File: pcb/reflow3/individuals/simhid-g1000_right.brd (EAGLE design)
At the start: 35 x 192 mm, 75 parts, among them J4 PCB-INTERCONNECT, J5 USB4145-03-0230-CHS, J6 2212S, SW27 SLLB510100-HS, SW28 TS-1109S-B-B, SW29 TS-1109S-B-B, SW30 TS-1109S-B-B, SW31 TS-1109S-B-B, SW32 TS-1109S-B-B, SW33 TS-1109S-B-B, SW34 TS-1109S-B-B, U4 STM32F411CCU, U5 MCP23S18-E/MJ, U6 MCP1703AT-3302E/CB, X1 16MHz/10pF

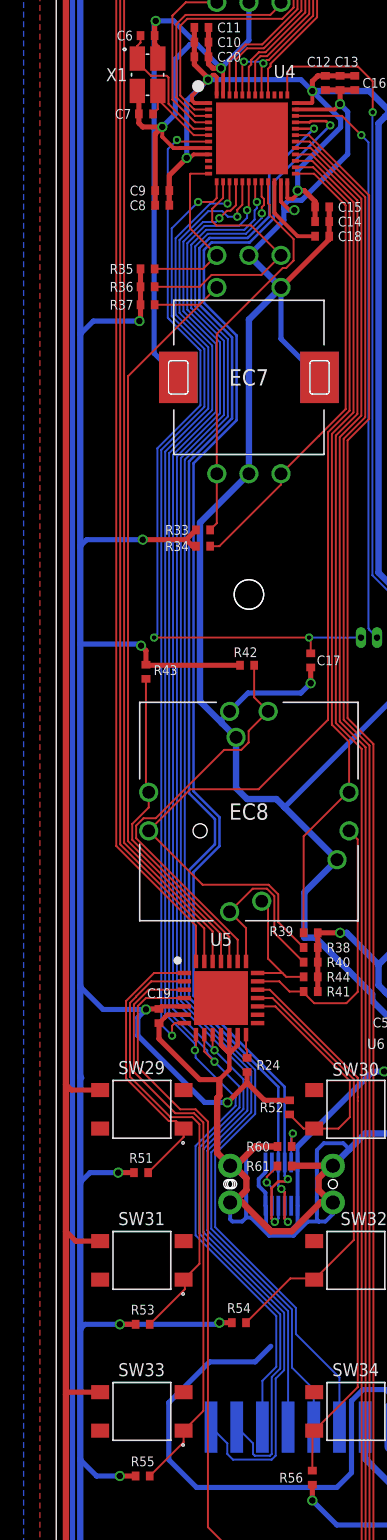
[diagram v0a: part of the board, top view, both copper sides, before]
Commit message: improved the artwork for the new variant
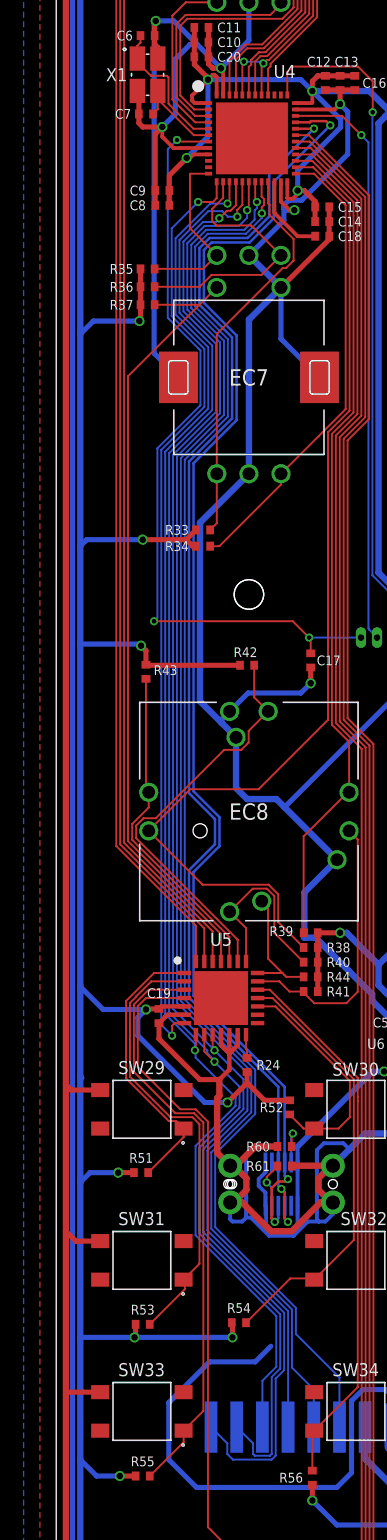
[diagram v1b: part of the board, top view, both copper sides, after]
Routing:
- net +3V3: track 611.1 -> 611.9 mm
- net NRST: track 61.5 -> 60.7 mm
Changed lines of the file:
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@@
 </layers>
 <board>
-<fusionsync huburn="a.cGVyc29uYWw6dWUyYmE2M2My" projecturn="a.cGVyc29uYWw6dWUyYmE2M2MyIzIwMTgwOTE3MTQ5MTY5Mjgx" f3durn="urn:adsk.wipprod:dm.lineage:6ddGwsoNRdCcNz8sAvQdYQ" pcbguid="" lastpulledtime="" lastsyncedchangeguid="" latestrevisionid="cc2a4dc4-e200-4016-af02-b88be0bf32b0" lastsyncedrevisionid="cc2a4dc4-e200-4016-af02-b88be0bf32b0" lastboardhashguid="d191e26a-343e-daae-d877-4dd18b740236" lastpushedtime="2021-09-07T03:43:09Z" linktopcb3d="false"/>
+<fusionsync huburn="a.cGVyc29uYWw6dWUyYmE2M2My" projecturn="a.cGVyc29uYWw6dWUyYmE2M2MyIzIwMTgwOTE3MTQ5MTY5Mjgx" f3durn="urn:adsk.wipprod:dm.lineage:6ddGwsoNRdCcNz8sAvQdYQ" pcbguid="" lastpulledtime="" lastsyncedchangeguid="" latestrevisionid="cc2a4dc4-e200-4016-af02-b88be0bf32b0" lastsyncedrevisionid="cc2a4dc4-e200-4016-af02-b88be0bf32b0" lastboardhashguid="d191e26a-343e-daae-d877-4dd18b740236" lastpushedtime="2021-09-07T03:43:09Z" linktopcb3d="true"/>
 <plain>
 <circle x="27" y="65.6757" radius="1.15" width="0" layer="20"/>
@@
 <wire x1="14.1096" y1="50.41" x2="14.79" y2="49.7296" width="0.3" layer="16"/>
 <wire x1="14.79" y1="49.7296" x2="14.79" y2="49.53" width="0.3" layer="16"/>
-<wire x1="15" y1="186.825" x2="15" y2="186.825" width="0" layer="19" extent="1-16"/>
-<wire x1="9.5" y1="148.901" x2="9.5" y2="148.901" width="0" layer="19" extent="1-16"/>
-<wire x1="9.5" y1="112.201" x2="9.5" y2="112.201" width="0" layer="19" extent="1-16"/>
-<wire x1="15" y1="15.5" x2="15" y2="15.5" width="0" layer="19" extent="1-16"/>
-<wire x1="15" y1="4.5" x2="15" y2="4.5" width="0" layer="19" extent="1-16"/>
-<wire x1="20.5" y1="148.901" x2="20.5" y2="148.901" width="0" layer="19" extent="1-16"/>
-<wire x1="20.5" y1="112.201" x2="20.5" y2="112.201" width="0" layer="19" extent="1-16"/>
-<wire x1="13.97" y1="50.8" x2="13.54" y2="50.827" width="0" layer="19" extent="1-1"/>
 </signal>
 <signal name="+3V3" class="2">
@@
 <wire x1="1.8724" y1="64.77" x2="1.8724" y2="57.785" width="0.5" layer="16"/>
 <wire x1="1.8724" y1="57.785" x2="1.8724" y2="49.53" width="0.5" layer="16"/>
-<wire x1="1.8724" y1="49.53" x2="1.8724" y2="38.1" width="0.5" layer="16"/>
-<wire x1="1.8724" y1="38.1" x2="1.8724" y2="27.94" width="0.5" layer="16"/>
+<wire x1="1.8724" y1="49.53" x2="1.8724" y2="37.465" width="0.5" layer="16"/>
+<wire x1="1.8724" y1="37.465" x2="1.8724" y2="27.94" width="0.5" layer="16"/>
 <wire x1="1.8724" y1="27.94" x2="1.8724" y2="17.78" width="0.5" layer="16"/>
 <wire x1="1.8724" y1="17.78" x2="1.8724" y2="8.2876" width="0.5" layer="16"/>
@@
 <wire x1="4.826" y1="50.292" x2="2.6344" y2="50.292" width="0.4" layer="16"/>
 <wire x1="2.6344" y1="50.292" x2="1.8724" y2="49.53" width="0.4" layer="16"/>
-<via x="4.953" y="38.481" extent="1-16" drill="0.5"/>
-<via x="12.7" y="38.608" extent="1-16" drill="0.5"/>
-<wire x1="13.674" y1="38.608" x2="12.7" y2="38.608" width="0.4" layer="1"/>
-<wire x1="6.181" y1="38.481" x2="4.953" y2="38.481" width="0.4" layer="1"/>
-<wire x1="12.7" y1="38.608" x2="12.573" y2="38.481" width="0.4" layer="16"/>
-<wire x1="12.573" y1="38.481" x2="4.953" y2="38.481" width="0.4" layer="16"/>
-<wire x1="4.953" y1="38.481" x2="2.2534" y2="38.481" width="0.4" layer="16"/>
-<wire x1="2.2534" y1="38.481" x2="1.8724" y2="38.1" width="0.4" layer="16"/>
+<via x="6.096" y="37.465" extent="1-16" drill="0.5"/>
+<via x="13.716" y="37.465" extent="1-16" drill="0.5"/>
+<wire x1="13.716" y1="37.465" x2="6.096" y2="37.465" width="0.4" layer="16"/>
+<wire x1="6.096" y1="37.465" x2="1.8724" y2="37.465" width="0.4" layer="16"/>
 <via x="4.953" y="26.67" extent="1-16" drill="0.5"/>
 <via x="19.939" y="24.765" extent="1-16" drill="0.5"/>
@@
 <wire x1="10.574096875" y1="133.764096875" x2="10.574096875" y2="134.145096875" width="0.3" layer="1"/>
 <wire x1="10.574096875" y1="134.145096875" x2="11.811" y2="135.382" width="0.3" layer="1"/>
-<wire x1="11.811" y1="135.382" x2="10.16" y2="133.731" width="0.4" layer="16"/>
-<wire x1="10.16" y1="133.731" x2="10.16" y2="129.286" width="0.4" layer="16"/>
 <wire x1="19.939" y1="134.493" x2="22.1428" y2="132.2892" width="0.4" layer="16"/>
 <wire x1="22.1428" y1="132.2892" x2="22.1428" y2="131.6714125" width="0.4" layer="16"/>
@@
 <wire x1="26.755" y1="61.849" x2="26.755" y2="62.569" width="0.5" layer="1"/>
 <wire x1="26.755" y1="62.569" x2="27.305" y2="63.119" width="0.5" layer="1"/>
+<wire x1="10.16" y1="129.286" x2="11.811" y2="130.937" width="0.4" layer="16"/>
+<wire x1="11.811" y1="130.937" x2="11.811" y2="135.382" width="0.4" layer="16"/>
+<wire x1="13.674" y1="38.608" x2="13.716" y2="38.566" width="0.4" layer="1"/>
+<wire x1="13.716" y1="38.566" x2="13.716" y2="37.465" width="0.4" layer="1"/>
+<wire x1="6.181" y1="38.481" x2="6.181" y2="37.55" width="0.4" layer="1"/>
+<wire x1="6.181" y1="37.55" x2="6.096" y2="37.465" width="0.4" layer="1"/>
 </signal>
 <signal name="USB_D-">
@@
 <wire x1="19.688" y1="91.945" x2="19.685" y2="91.948" width="0.1524" layer="16"/>
 <via x="19.685" y="91.948" extent="1-16" drill="0.35"/>
-<wire x1="19.685" y1="91.948" x2="7.62" y2="91.948" width="0.1524" layer="1"/>
-<via x="7.62" y="91.948" extent="1-16" drill="0.35"/>
-<wire x1="7.8738" y1="92.2018" x2="7.62" y2="91.948" width="0.1524" layer="16"/>
-<wire x1="7.8738" y1="106.6798" x2="7.8738" y2="92.2018" width="0.1524" layer="16"/>
+<wire x1="19.685" y1="91.948" x2="18.415" y2="93.218" width="0.1524" layer="1"/>
+<wire x1="18.415" y1="93.218" x2="7.62" y2="93.218" width="0.1524" layer="1"/>
+<via x="7.62" y="93.218" extent="1-16" drill="0.35"/>
+<wire x1="7.8738" y1="93.4718" x2="7.62" y2="93.218" width="0.1524" layer="16"/>
+<wire x1="7.8738" y1="106.6798" x2="7.8738" y2="93.4718" width="0.1524" layer="16"/>
 <wire x1="8.7865" y1="116.7377875" x2="8.683" y2="116.8412875" width="0.1524" layer="16"/>
 <wire x1="8.7865" y1="116.7377875" x2="8.7865" y2="116.7365" width="0.1524" layer="16"/>

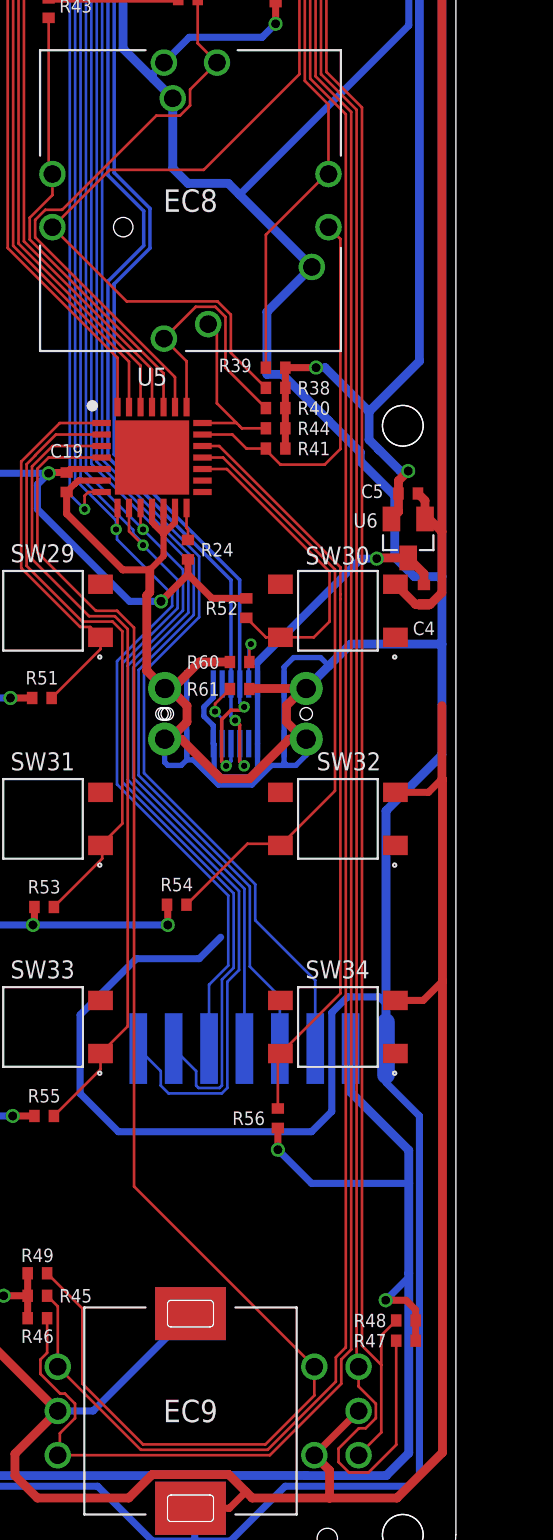
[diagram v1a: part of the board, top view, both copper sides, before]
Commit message: Modify the PCB design for USB Type-C
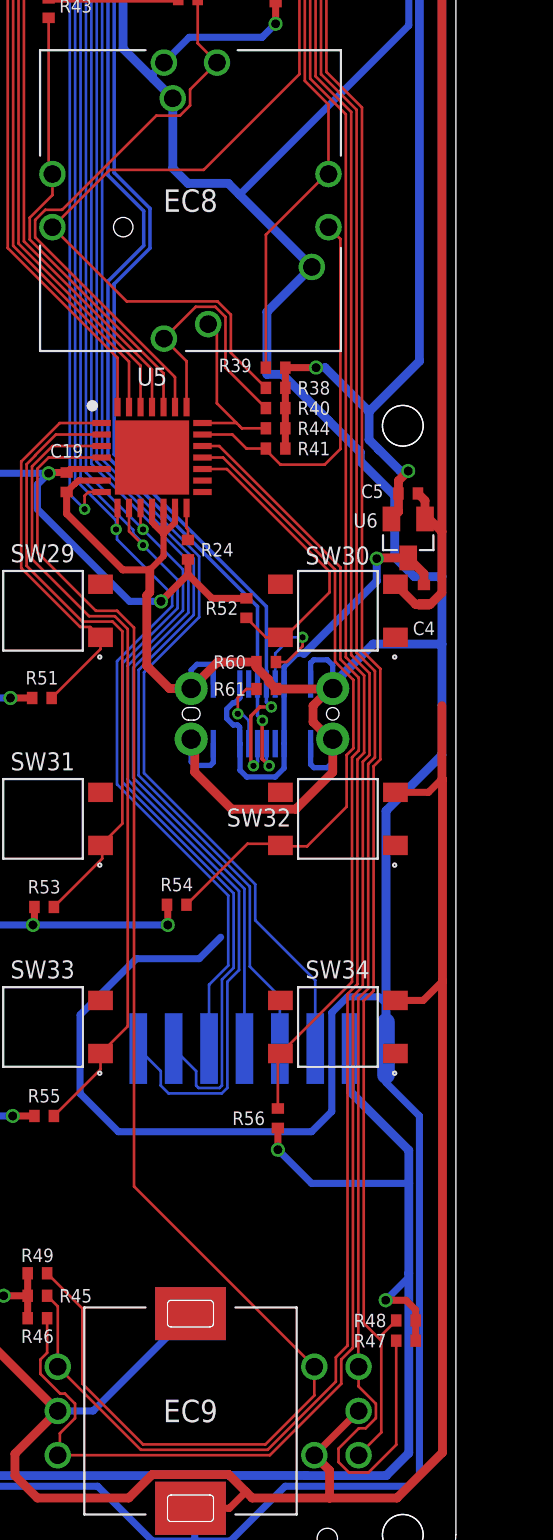
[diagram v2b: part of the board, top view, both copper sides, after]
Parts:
- moved J5 1.50 mm to (19.0, 49.4)
- moved R60 1.50 mm to (19.3, 52.3)
- moved R61 1.50 mm to (19.3, 50.8)
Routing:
- net GND: track 1339.5 -> 1330.4 mm
- net N$3: track 3.36 -> 6.03 mm
- net SW32: track 33.8 -> 35.7 mm
- net SW30: track 17.9 -> 17.0 mm
- net EC9_YA: track 139.5 -> 140.3 mm
- net EC9_XB: track 150.0 -> 150.9 mm
- net SW34: track 42.7 -> 43.5 mm
- net EC9_XA: track 145.9 -> 146.8 mm
- net N$4: track 3.60 -> 4.25 mm
- net EC9_YB: track 131.9 -> 131.3 mm
- net USB_D+: track 103.6 -> 104.1 mm
- net USB_D-: track 100.7 -> 101.2 mm
